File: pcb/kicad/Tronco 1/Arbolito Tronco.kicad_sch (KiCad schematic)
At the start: 26 parts, among them J1 Conn_01x01, J10 Conn_01x01, J11 Conn_01x01, J12 Conn_01x01, J2 Conn_01x01, J3 Conn_01x01, J4 Conn_01x01, J5 Conn_01x01, J6 Conn_01x01, J7 Conn_01x01, J8 Conn_01x01, J9 Conn_01x01, U1 WS2812B, U2 WS2812B, U3 WS2812B, U4 WS2812B, U5 WS2812B, U6 WS2812B, U7 WS2812B, U8 WS2812B

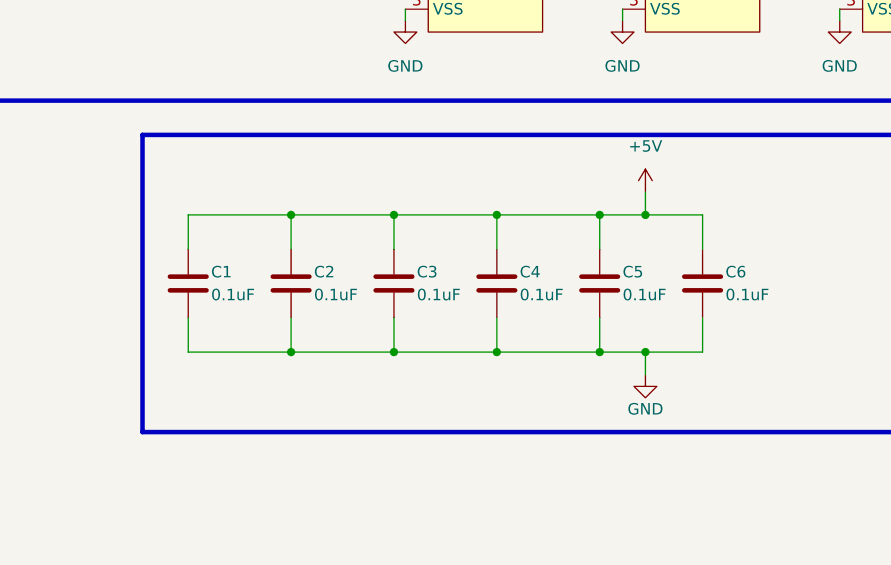
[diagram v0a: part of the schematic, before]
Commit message: Added Rev3 release files
- Added ibom html files
- Update ibom in .web directory
- Update pdf schematics
- Added 3D steps files
- Added tools for help to mount the PCB
- Added hw rev3 gerber files
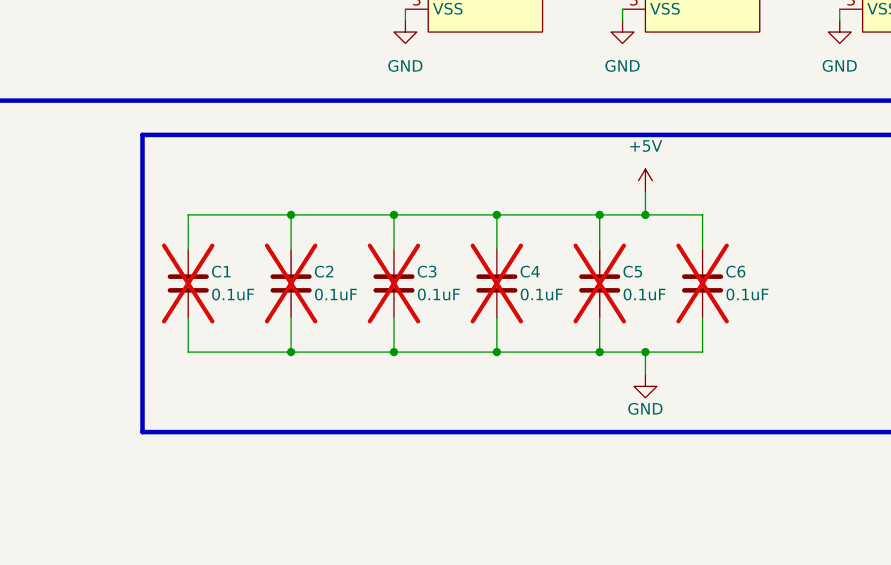
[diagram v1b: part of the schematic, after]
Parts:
- C1, C2, C3, C4, C5, C6: now not fitted
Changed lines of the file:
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@@
   )
   (symbol (lib_id "Device:C") (at 88.9 119.38 0) (unit 1)
-    (in_bom yes) (on_board yes) (dnp no)
+    (in_bom yes) (on_board yes) (dnp yes)
     (property "Reference" "C2" (at 91.44 118.11 0)
       (effects (font (size 1.27 1.27)) (justify left))
@@
   )
   (symbol (lib_id "Device:C") (at 123.19 119.38 0) (unit 1)
-    (in_bom yes) (on_board yes) (dnp no)
+    (in_bom yes) (on_board yes) (dnp yes)
     (property "Reference" "C5" (at 125.73 118.11 0)
       (effects (font (size 1.27 1.27)) (justify left))
@@
   )
   (symbol (lib_id "Device:C") (at 134.62 119.38 0) (unit 1)
-    (in_bom yes) (on_board yes) (dnp no)
+    (in_bom yes) (on_board yes) (dnp yes)
     (property "Reference" "C6" (at 137.16 118.11 0)
       (effects (font (size 1.27 1.27)) (justify left))
@@
   )
   (symbol (lib_id "Device:C") (at 77.47 119.38 0) (unit 1)
-    (in_bom yes) (on_board yes) (dnp no)
+    (in_bom yes) (on_board yes) (dnp yes)
     (property "Reference" "C1" (at 80.01 118.11 0)
       (effects (font (size 1.27 1.27)) (justify left))
@@
   )
   (symbol (lib_id "Device:C") (at 100.33 119.38 0) (unit 1)
-    (in_bom yes) (on_board yes) (dnp no)
+    (in_bom yes) (on_board yes) (dnp yes)
     (property "Reference" "C3" (at 102.87 118.11 0)
       (effects (font (size 1.27 1.27)) (justify left))
@@
   )
   (symbol (lib_id "Device:C") (at 111.76 119.38 0) (unit 1)
-    (in_bom yes) (on_board yes) (dnp no)
+    (in_bom yes) (on_board yes) (dnp yes)
     (property "Reference" "C4" (at 114.3 118.11 0)
       (effects (font (size 1.27 1.27)) (justify left))
